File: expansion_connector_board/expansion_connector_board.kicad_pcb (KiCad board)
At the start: 2 copper layers, 139 x 89 mm, 6 parts, among them J1 Conn_01x04, J12 Conn_02x17_Top_Bottom, J13 Conn_01x04, J3 Conn_02x17_Top_Bottom

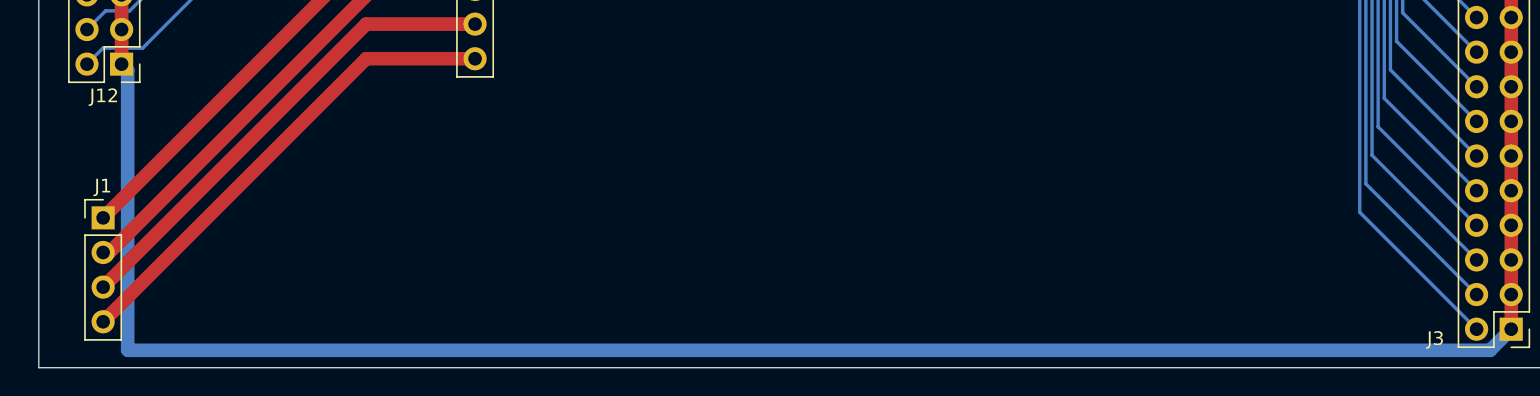
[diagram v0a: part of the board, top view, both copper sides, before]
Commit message: update floppy header names to match underlying boards
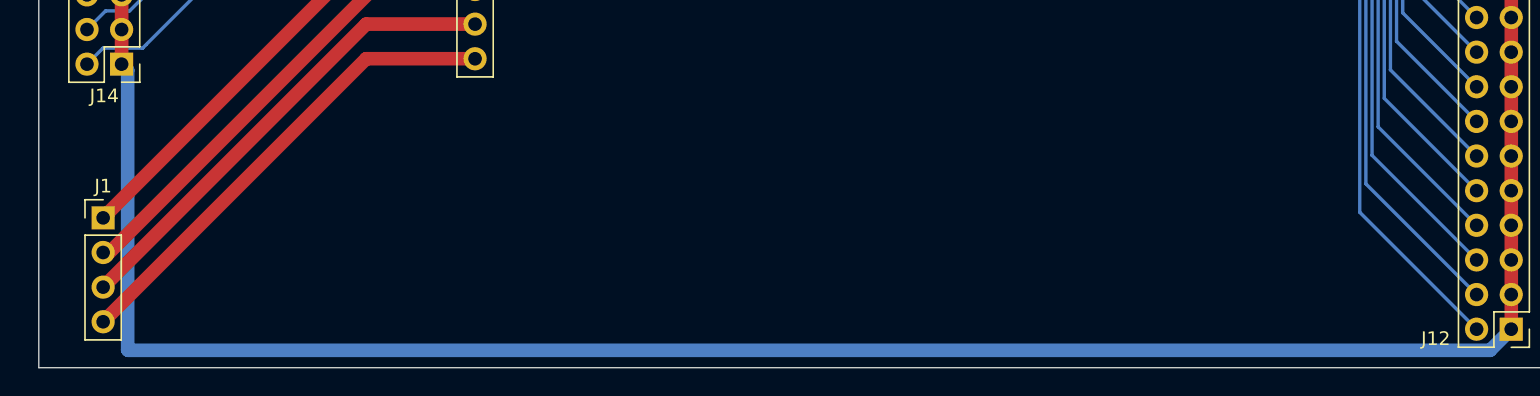
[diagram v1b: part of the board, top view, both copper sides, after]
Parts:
- renumbered J3 to J12, J12 to J14

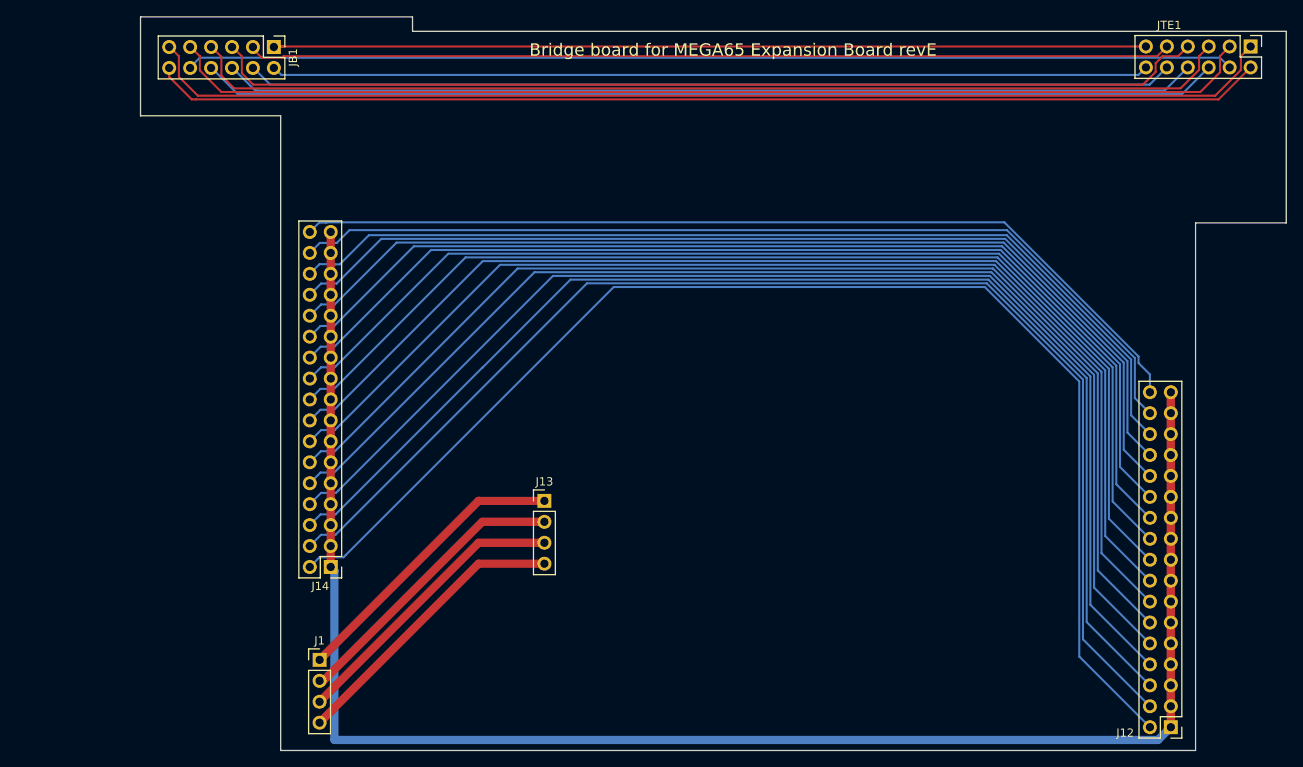
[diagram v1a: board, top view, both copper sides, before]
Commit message: update to kicad 7. begin adding ESP32
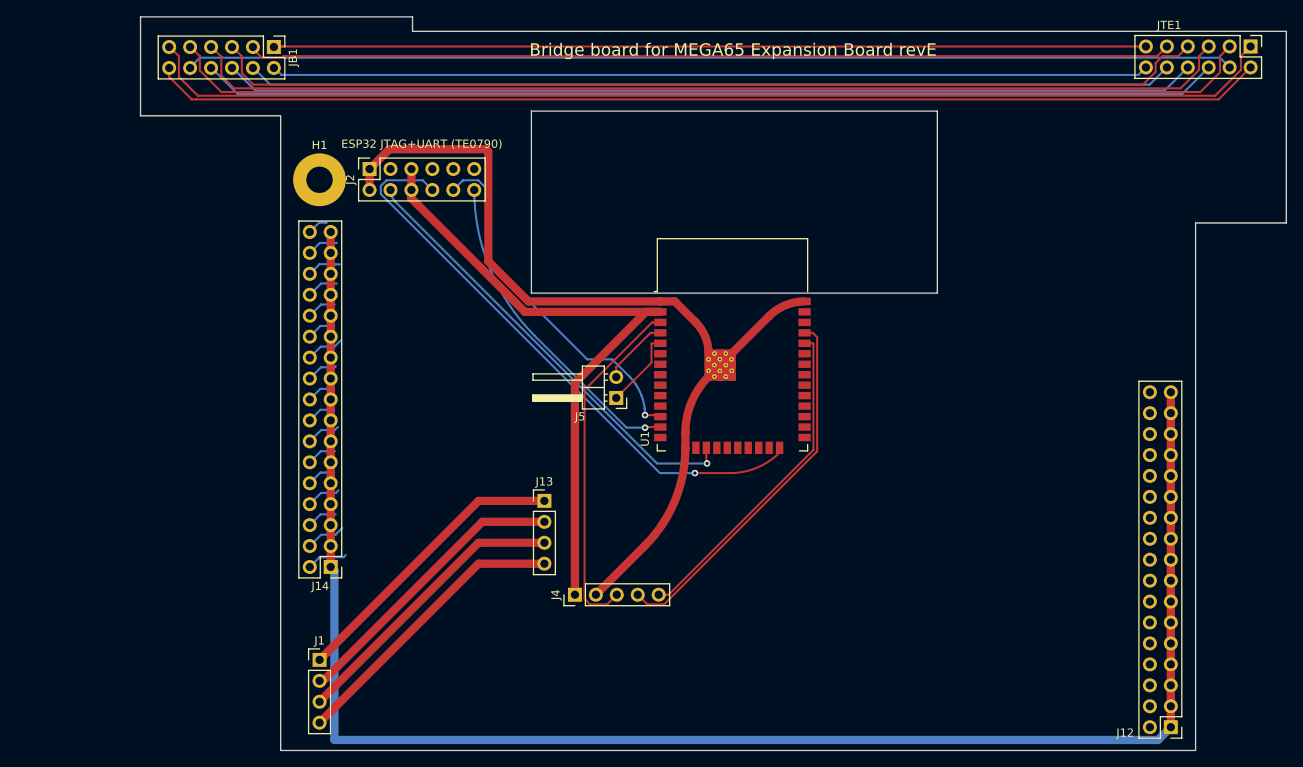
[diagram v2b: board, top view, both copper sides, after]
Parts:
- added H1: TE0790 Orienting Hole for ESP32 JTAG, MountingHole:MountingHole_3.2mm_M3_Pad, F.Cu at (78.7, 54.8)
- added J2: ESP32 JTAG+UART (TE0790), Connector_PinHeader_2.54mm:PinHeader_2x06_P2.54mm_Vertical, F.Cu at (84.8, 56.1)
- added J4: ESP32/Peripheral UART Interface, Connector_PinHeader_2.54mm:PinHeader_1x05_P2.54mm_Vertical, F.Cu at (109.7, 105.1)
- added J5: Conn_01x02, Connector_PinHeader_2.54mm:PinHeader_1x02_P2.54mm_Horizontal, F.Cu at (114.7, 81.2)
- added U1: ESP32-WROOM-32D, RF_Module:ESP32-WROOM-32D, F.Cu at (128.8, 77.8)
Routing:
- net Net-(J12-Pin_2): track 157.7 -> 4.95 mm
- net Net-(J12-Pin_4): track 154.8 -> 4.84 mm
- net Net-(J12-Pin_6): track 152.0 -> 3.67 mm
- net Net-(J12-Pin_8): track 149.2 -> 4.18 mm
- net Net-(J12-Pin_10): track 146.3 -> 3.49 mm
- net Net-(J12-Pin_12): track 143.5 -> 3.61 mm
- net Net-(J12-Pin_14): track 140.6 -> 4.13 mm
- net Net-(J12-Pin_16): track 137.8 -> 3.49 mm
- net Net-(J12-Pin_18): track 134.9 -> 3.48 mm
- net Net-(J12-Pin_20): track 132.1 -> 3.78 mm
- net Net-(J12-Pin_22): track 129.2 -> 4.59 mm
- net Net-(J12-Pin_24): track 126.4 -> 3.50 mm
- net Net-(J12-Pin_26): track 123.5 -> 3.59 mm
- net Net-(J12-Pin_28): track 120.7 -> 3.82 mm
- net Net-(J12-Pin_30): track 118.6 -> 4.84 mm
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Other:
- outline, holes or cut-outs redrawn

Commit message: finish adding ESP32 to bridge board
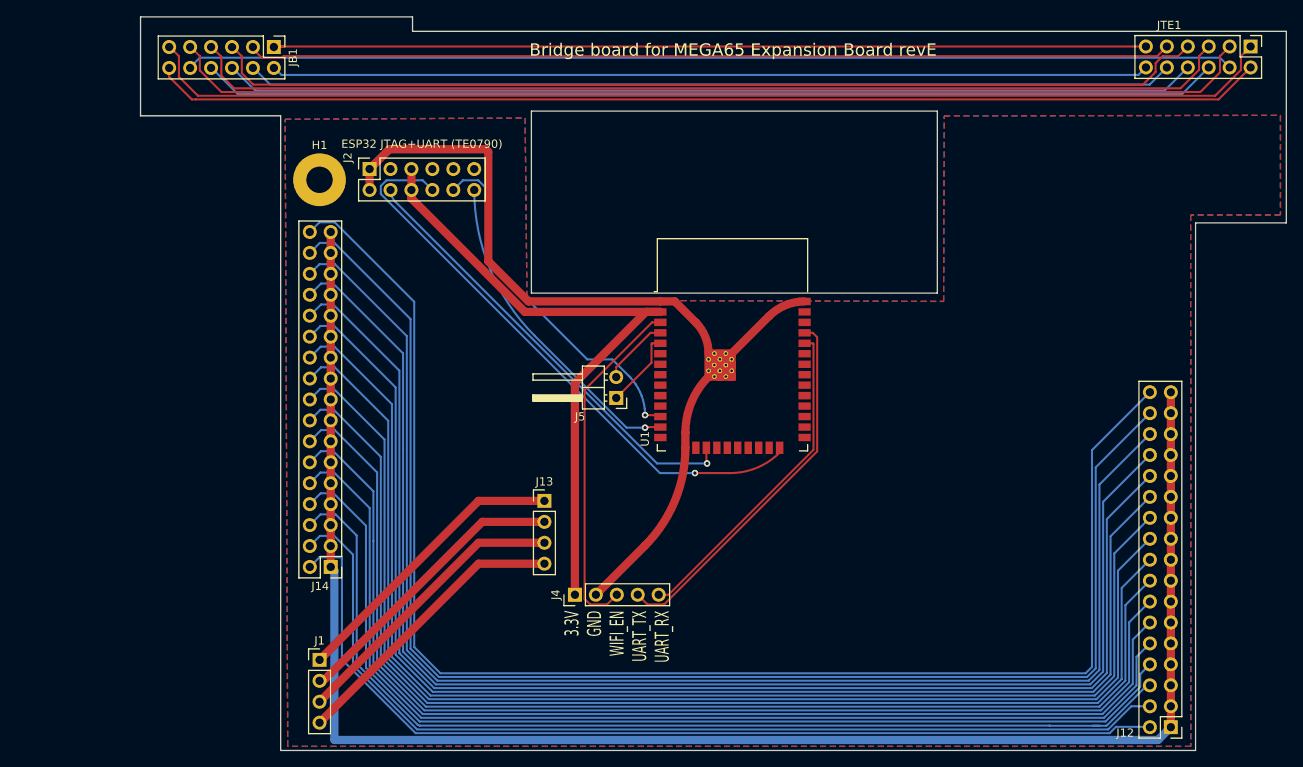
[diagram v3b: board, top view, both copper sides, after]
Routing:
- net Net-(J12-Pin_34): track 3.25 -> 179.8 mm
- net Net-(J12-Pin_32): track 4.49 -> 175.9 mm
- net Net-(J12-Pin_30): track 4.84 -> 171.9 mm
- net Net-(J12-Pin_28): track 3.82 -> 167.4 mm
- net Net-(J12-Pin_26): track 3.59 -> 163.5 mm
- net Net-(J12-Pin_24): track 3.50 -> 159.5 mm
- net Net-(J12-Pin_22): track 4.59 -> 155.6 mm
- net Net-(J12-Pin_20): track 3.78 -> 151.7 mm
- net Net-(J12-Pin_18): track 3.48 -> 147.9 mm
- net Net-(J12-Pin_16): track 3.49 -> 143.9 mm
- net Net-(J12-Pin_14): track 4.13 -> 139.9 mm
- net Net-(J12-Pin_12): track 3.61 -> 135.8 mm
- net Net-(J12-Pin_10): track 3.49 -> 131.8 mm
- net Net-(J12-Pin_8): track 4.18 -> 127.8 mm
- net Net-(J12-Pin_6): track 3.67 -> 125.3 mm
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- added copper zone on B.Cu, net GND
- added copper zone on F.Cu, net GND
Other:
- board text added: "3.3V GND WIFI_EN UART_TX UART_RX"

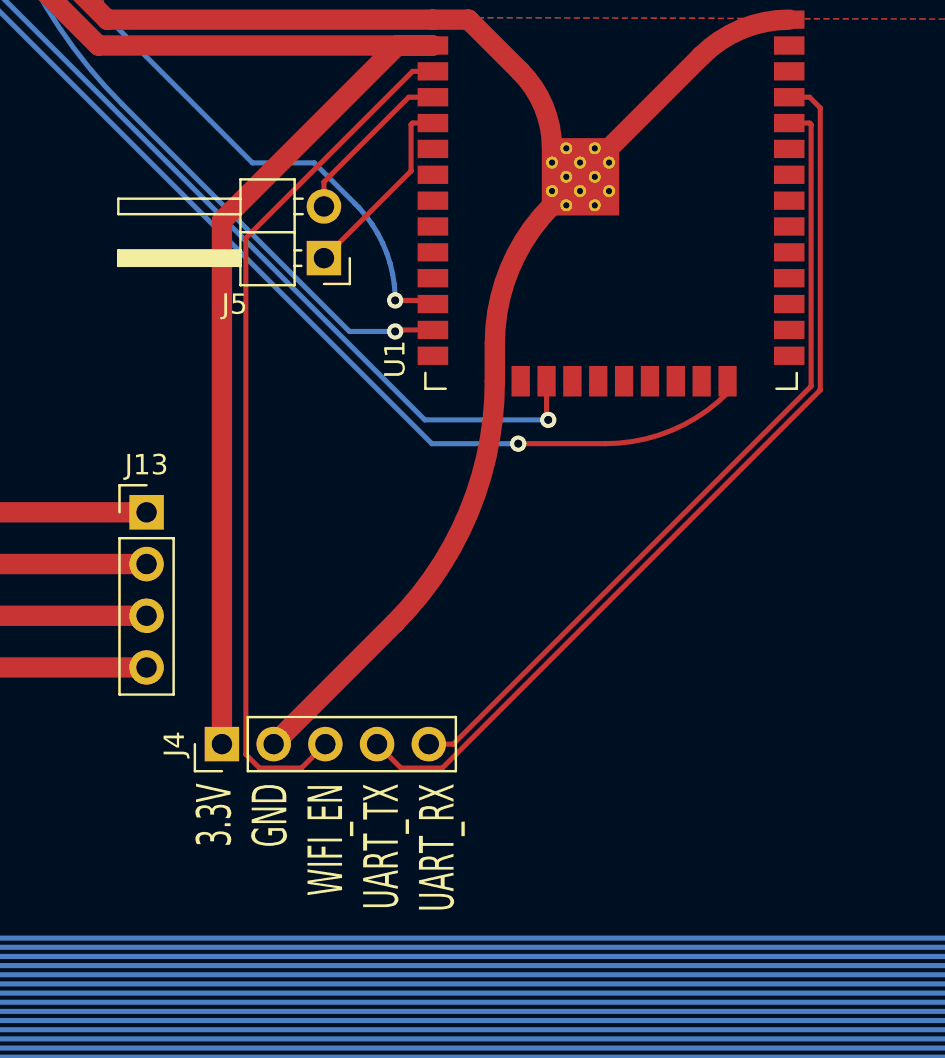
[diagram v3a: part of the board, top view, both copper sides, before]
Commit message: add more pins to peripheral header. Reorder
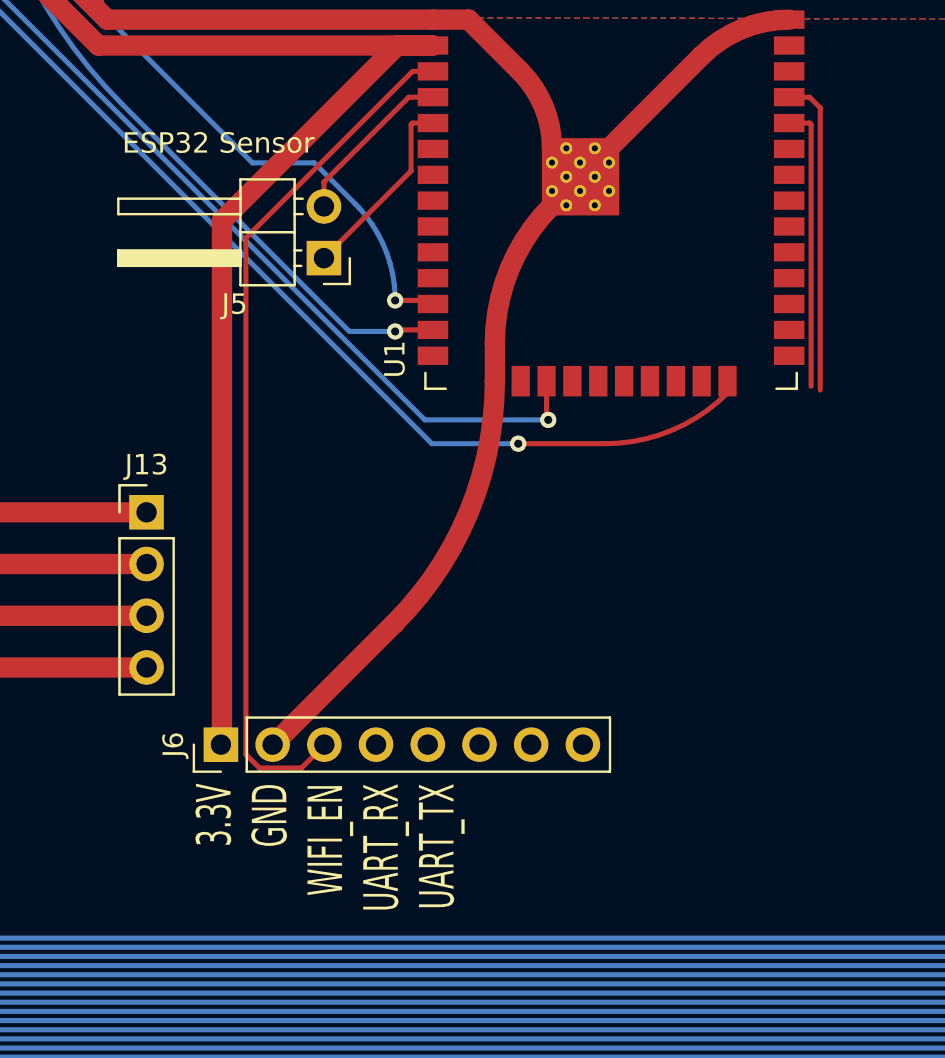
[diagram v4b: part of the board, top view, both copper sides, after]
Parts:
- removed J4: ESP32/Peripheral UART Interface, Connector_PinHeader_2.54mm:PinHeader_1x05_P2.54mm_Vertical
- added J6: ESP32/Peripheral UART Interface, Connector_PinHeader_2.54mm:PinHeader_1x08_P2.54mm_Vertical, F.Cu at (109.7, 105.1)
- J5: value Conn_01x02 -> ESP32 Sensor
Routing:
- net UART_TX: track 45.5 -> 15.6 mm
- net UART_RX: track 40.0 -> 14.0 mm
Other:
- board text added: "3.3V GND WIFI_EN UART_RX UART_TX"
- board text added: "ESP32 Sensor"
- board text removed: "3.3V GND WIFI_EN UART_TX UART_RX"

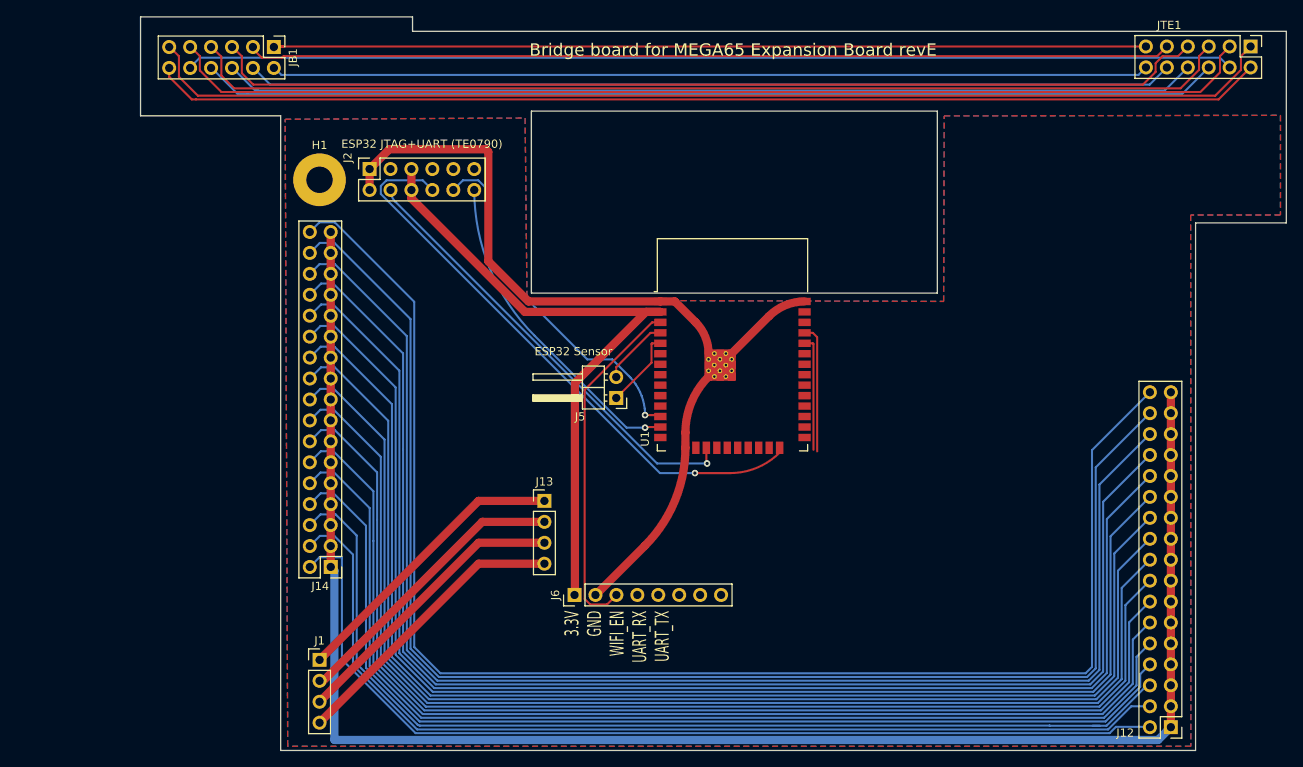
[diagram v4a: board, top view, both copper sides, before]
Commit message: add remaining connectors to bridge board
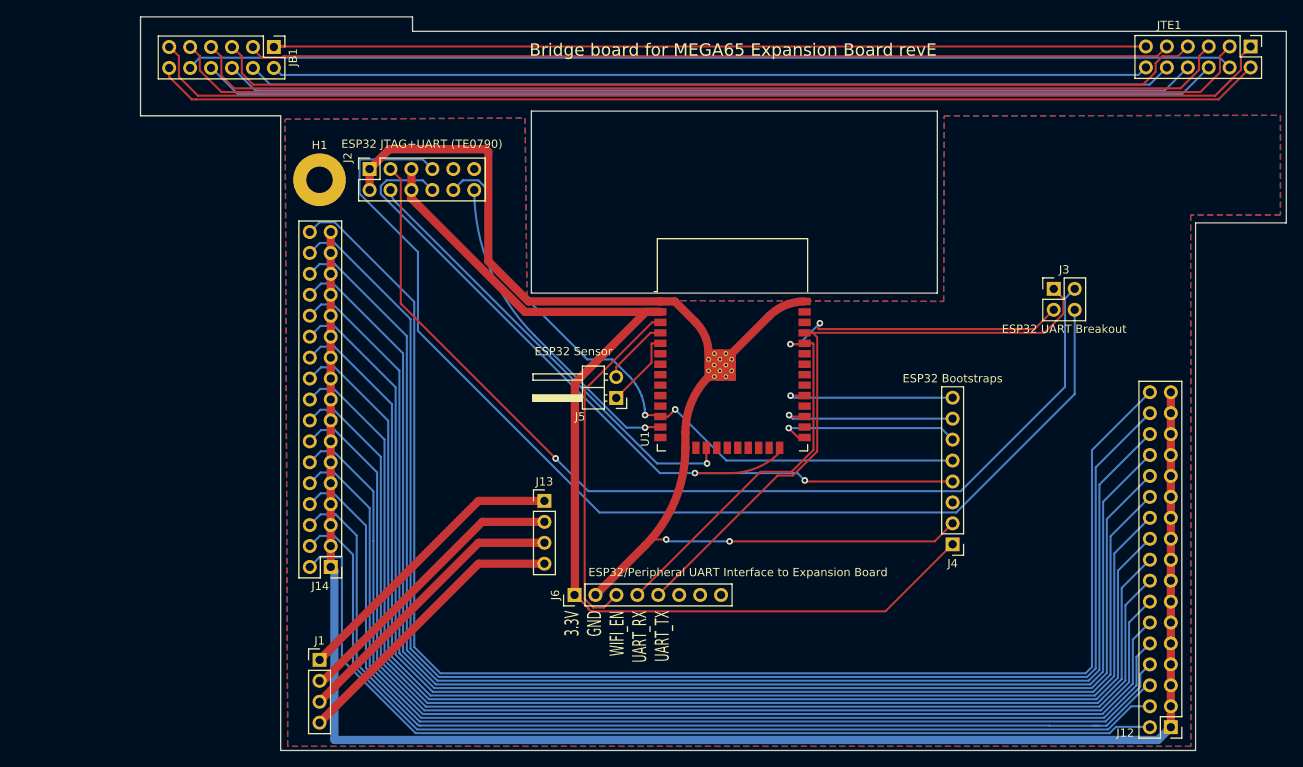
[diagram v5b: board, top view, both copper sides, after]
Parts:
- added J3: ESP32 UART Breakout, Connector_PinHeader_2.54mm:PinHeader_2x02_P2.54mm_Vertical, F.Cu at (167.8, 68.0)
- added J4: ESP32 Bootstraps, Connector_PinHeader_2.54mm:PinHeader_1x08_P2.54mm_Vertical, F.Cu at (155.5, 99.0)
- J6: value ESP32/Peripheral UART Interface -> ESP32/Peripheral UART Interface to Expansion Board
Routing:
- net /TE0790_B: track 0.00 -> 138.0 mm
- net /TE0790_A: track 0.00 -> 124.5 mm, vias 0 -> 1
- net UART_RX: track 14.0 -> 79.3 mm, vias 0 -> 2
- net UART_TX: track 15.6 -> 78.0 mm
- net +3.3V: track 79.1 -> 129.6 mm
- net JTAG_MTDI: track 43.7 -> 82.1 mm, vias 1 -> 2
- net GND: track 105.8 -> 143.4 mm, vias 0 -> 2
- net JTAG_MTDO: track 71.6 -> 103.3 mm, vias 1 -> 2
- net BOOT_STRAP0: track 0.00 -> 22.9 mm, vias 0 -> 1
- net BOOT_OPTION: track 0.00 -> 22.0 mm, vias 0 -> 1
- net BOOT_STRAP5: track 0.00 -> 21.5 mm, vias 0 -> 1
